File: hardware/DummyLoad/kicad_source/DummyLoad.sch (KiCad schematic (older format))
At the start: 53 parts, among them CN1 CON-SMA-EDGE-S-ND, CN2 CON-SMA-EDGE-S-ND

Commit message: added pdf files, licence files, gerber files. updated data for release, generated zip file
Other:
- note added: "Copyright generationmake 2019\nsee full project documentation at http://ardutrx.generationmake.de"
- note added: "You may redistribute and modify this documentation under the terms of the CERN OHL v.1.2. (http://ohwr.org/cernohl).\nThis documentation is distributed WITHOUT ANY EXPRESS OR IMPLIED WARRANTY, INCLUDING OF MERCHANTABILITY, SATISFACTORY\nQUALITY AND FITNESS FOR A PARTICULAR PURPOSE. Please see the CERN OHL v.1.2 for applicable conditions"
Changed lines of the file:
@@
 encoding utf-8
 Sheet 1 1
-Title ""
-Date ""
-Rev ""
-Comp ""
+Title "ArduTrx Dummy Load"
+Date "2019-05-30"
+Rev "1.0"
+Comp "generationmake"
 Comment1 ""
 Comment2 ""
 Comment3 ""
-Comment4 ""
+Comment4 "This documentation describes Open Hardware and is licensed under the CERN OHL v. 1.2."
 $EndDescr
 $Comp
@@
 Text Notes 1500 6350 0    50   ~ 0
 use standard 0805 resistors with 125 mW to get a 6,25 W dummy load\nuse Digikey P16057CT-ND resistors with 500 mW to get a 25 W dummy load
+Text Notes 750  800  0    50   ~ 0
+Copyright generationmake 2019\nsee full project documentation at http://ardutrx.generationmake.de
+Text Notes 7000 6900 0    43   ~ 0
+You may redistribute and modify this documentation under the terms of the CERN OHL v.1.2. (http://ohwr.org/cernohl).\nThis documentation is distributed WITHOUT ANY EXPRESS OR IMPLIED WARRANTY, INCLUDING OF MERCHANTABILITY, SATISFACTORY\nQUALITY AND FITNESS FOR A PARTICULAR PURPOSE. Please see the CERN OHL v.1.2 for applicable conditions
 $EndSCHEMATC

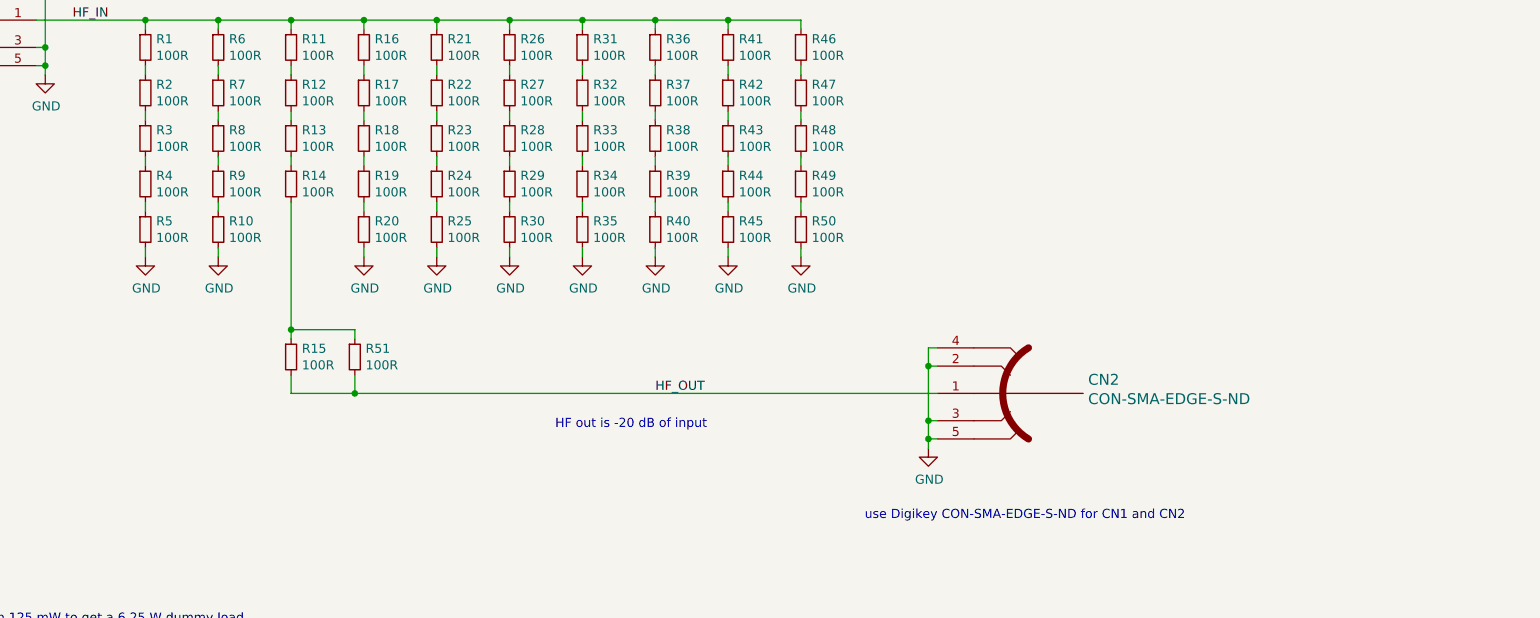
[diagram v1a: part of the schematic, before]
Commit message: reworked schematic to have 50 ohms on input and output
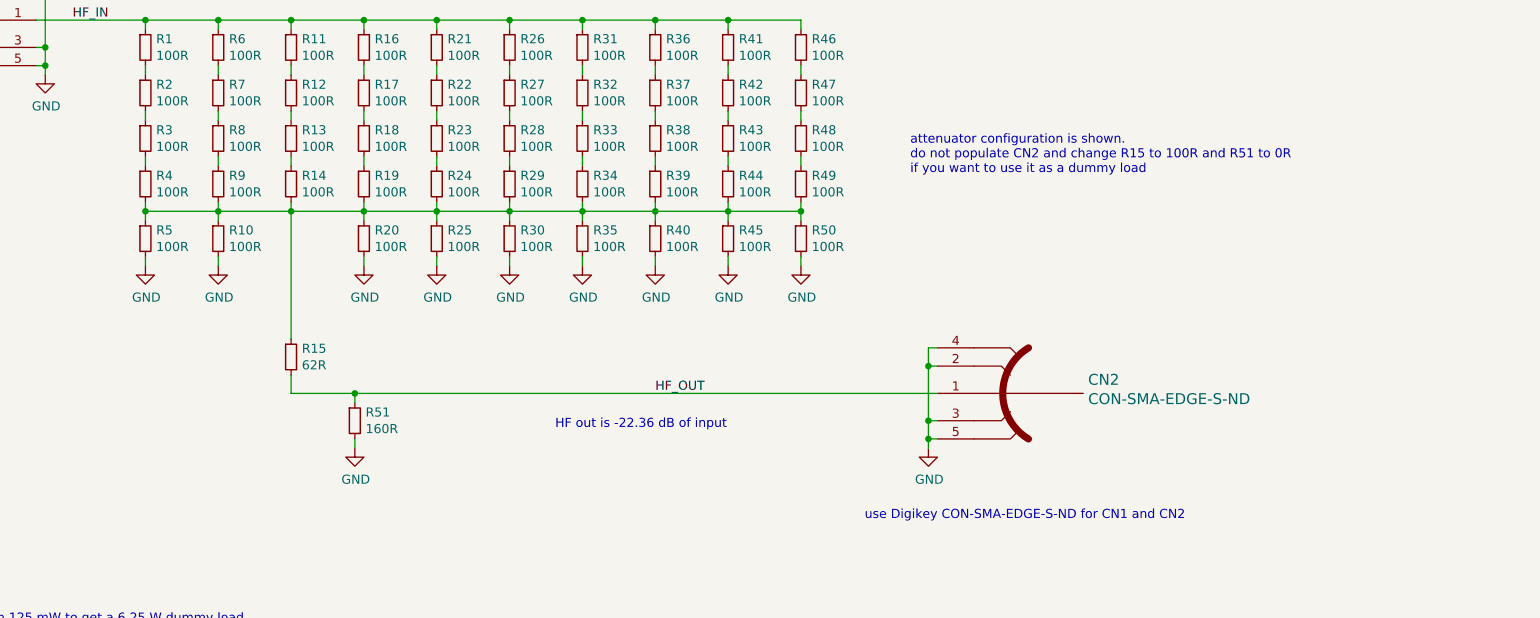
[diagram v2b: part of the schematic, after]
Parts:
- R15: value 100R -> 62R
- R51: value 100R -> 160R
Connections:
- net GND: now also R51.2
- net HF_OUT: now also R51.1; no longer R51.2
- net at R4.2, R5.1: now also R10.1, R14.2, R15.1, R19.2, R20.1, R24.2, R25.1, R29.2, R30.1, R34.2, R35.1, R39.2, R40.1, R44.2, R45.1, R49.2, R50.1, R9.2
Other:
- note added: "HF out is -22.36 dB of input"
- note added: "attenuator configuration is shown. \ndo not populate CN2 and change R15 to 100R and R51 to 0R \nif you want to use it as a dummy load"
- note removed: "HF out is -20 dB of input"
- moved on the sheet: R10, R20, R25, R30, R35, R40, R45, R5, R50, R51
